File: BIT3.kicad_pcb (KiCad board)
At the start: 2 copper layers, 121.3 x 109.4 mm, 49 parts, among them J1 Conn_02x04_Odd_Even, J2 Conn_01x02_Pin, J3 Conn_01x04_Socket, J4 Conn_02x02_Odd_Even, Q1 BSP89, SW1 SW_SPDT, SW2 SW_Push, SW3 SW_Push, U2 FODM217A, U3 FODM217A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

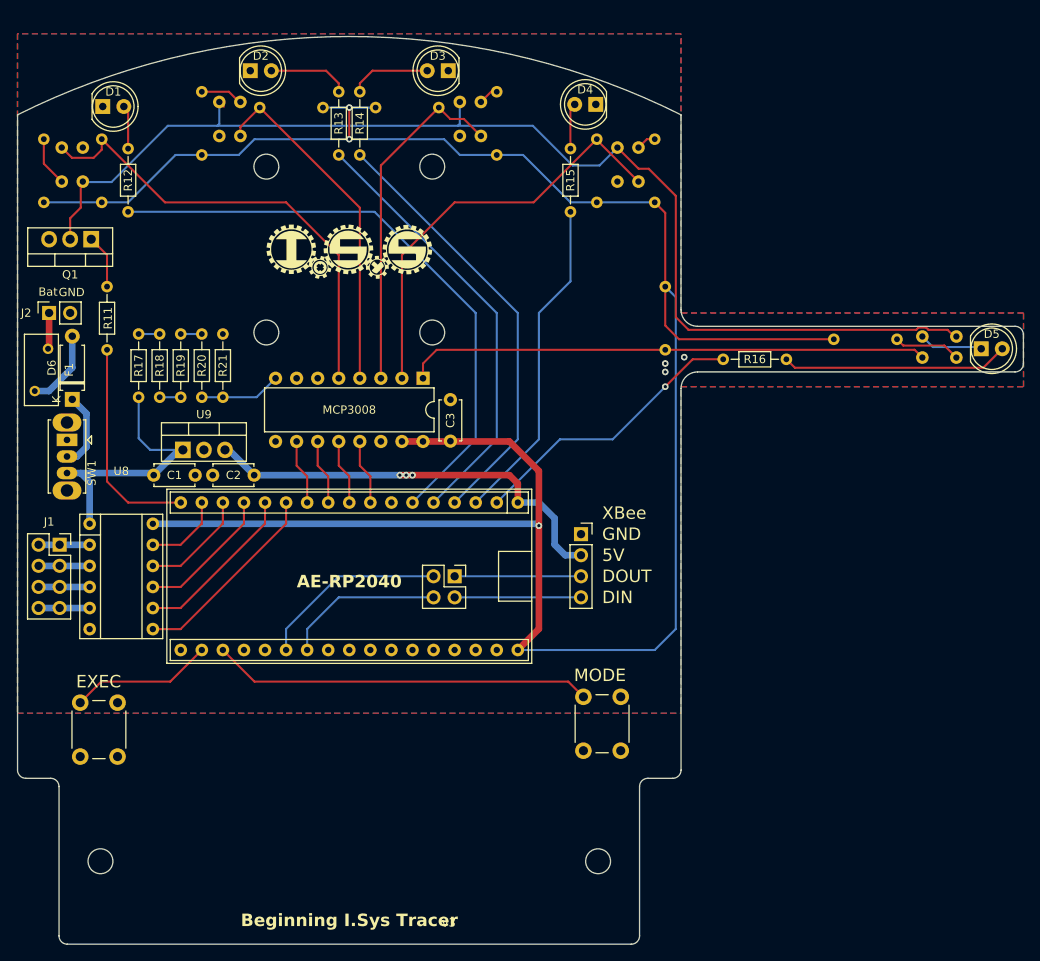
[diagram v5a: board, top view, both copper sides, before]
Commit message: 7 セグメント LED 用フットプリントを追加
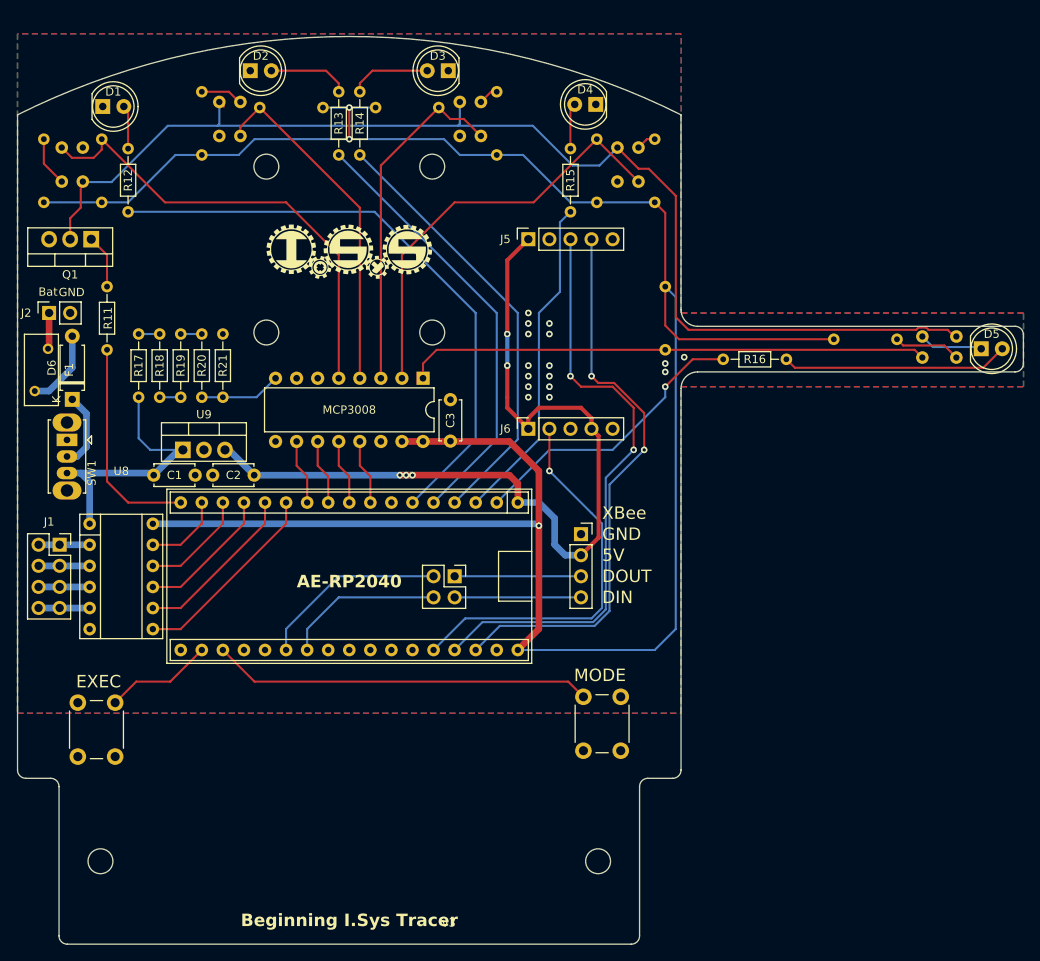
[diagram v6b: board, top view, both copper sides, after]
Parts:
- added J5: Conn_01x05_Socket, Connector_PinSocket_2.54mm:PinSocket_1x05_P2.54mm_Vertical, F.Cu at (174.0, 63.5)
- added J6: Conn_01x05_Socket, Connector_PinSocket_2.54mm:PinSocket_1x05_P2.54mm_Vertical, F.Cu at (174.0, 86.4)
- moved SW3 7.74 mm to (124.2, 119.4), turned to -90 degrees
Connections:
- U1 pad 30: unconnected-(U1-GPIO27-Pad30) -> /LATCH
- U1 pad 31: unconnected-(U1-GPIO28-Pad31) -> /SCK
- U1 pad 32: unconnected-(U1-GPIO29-Pad32) -> /SDI
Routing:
- net /SCK: track 0.00 -> 71.7 mm, vias 0 -> 2
- net /SDI: track 0.00 -> 68.4 mm, vias 0 -> 2
- net +5V: track 52.9 -> 105.6 mm, vias 3 -> 5
- net /LATCH: track 0.00 -> 46.6 mm, vias 0 -> 1
- net /BACK: track 17.3 -> 13.1 mm
- net /LED_Goal: track 34.5 -> 35.2 mm
- net GND: vias 3 -> 16

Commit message: センサ位置修正
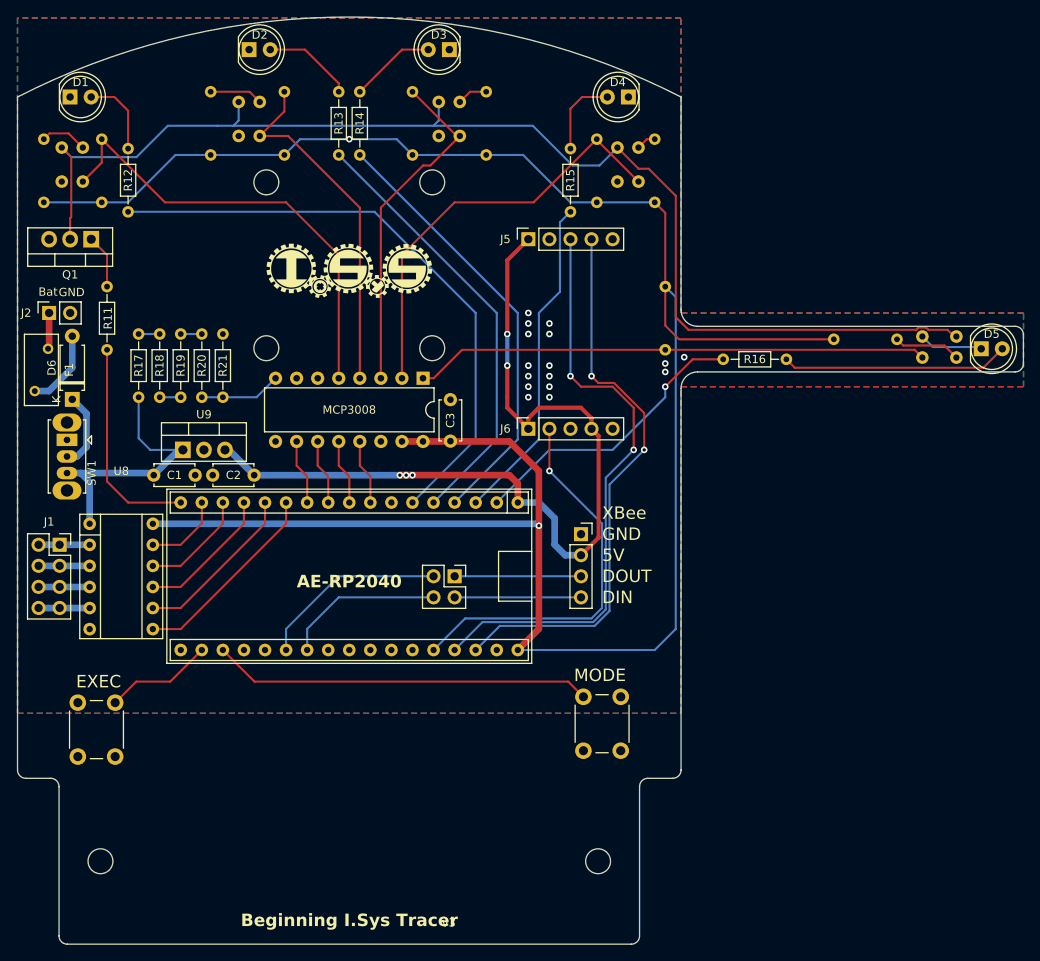
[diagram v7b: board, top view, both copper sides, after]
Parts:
- moved R8 7.37 mm to (144.6, 53.3), turned to 90 degrees
- moved R7 7.24 mm to (160.0, 53.3), turned to 90 degrees
- moved D1 4.10 mm to (118.7, 46.4)
- moved D4 4.03 mm to (186.1, 46.4)
- moved D2 2.54 mm to (140.3, 40.6)
- moved D3 2.54 mm to (164.5, 40.6)
- moved U4 2.54 mm to (164.5, 49.0)
- moved U3 2.34 mm to (140.3, 49.0)
- moved G*** 2.31 mm to (152.4, 67.3)
- moved R2 1.27 mm to (168.9, 53.3)
- moved R3 1.06 mm to (135.7, 53.3)
- turned U2 to 180 degrees
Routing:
- net +3V3: track 275.7 -> 265.5 mm, vias 3 -> 2
- net /FET_D: track 143.8 -> 149.0 mm
- net Net-(D1-A): track 5.29 -> 9.71 mm
- net Net-(D4-A): track 5.55 -> 9.85 mm
- net Net-(R3-Pad2): track 4.93 -> 6.43 mm
- net Net-(R2-Pad2): track 2.42 -> 3.69 mm
- net Net-(D2-A): track 9.78 -> 11.0 mm
- net /sensor_Goal: track 63.1 -> 62.0 mm
- net /sensor_CL: track 42.0 -> 42.8 mm
- net /sensor_L: track 56.2 -> 55.6 mm
- net Net-(D3-A): track 9.78 -> 10.4 mm
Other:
- board size 121.3 x 109.4 mm -> 121.3 x 111.8 mm

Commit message: センサ位置調整
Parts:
- moved R3 1.27 mm to (137.0, 53.2)
- moved R8 1.27 mm to (145.8, 53.2)
- moved U3 1.27 mm to (141.6, 48.9)
- moved U4 1.27 mm to (163.2, 48.9)
- moved R7 1.27 mm to (158.8, 53.3)
- moved R2 1.26 mm to (167.6, 53.3)
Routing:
- net /V_Battery: track 32.8 -> 35.8 mm
- net /sensor_CL: track 42.8 -> 41.6 mm
- net /sensor_CR: track 41.6 -> 40.6 mm
